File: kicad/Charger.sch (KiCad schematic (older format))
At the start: 14 parts, among them P7 USB_A, P8 BAT1, P9 BAT2, U10 MCP73831, U9 MCP73831

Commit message: 新基板，部品を配置
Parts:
- renumbered D14 to D16, D15 to D17, R23 to R25, R24 to R26, R25 to R27, R26 to R28
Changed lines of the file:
@@
 $EndComp
 $Comp
-L R R25
+L R R27
 U 1 1 58402BC3
 P 4300 4250
-AR Path="/58401A83/58402BC3" Ref="R25"  Part="1"
-AR Path="/58410148/58402BC3" Ref="R29"  Part="1"
-F 0 "R29" V 4380 4250 50  0000 C CNN
+AR Path="/58401A83/58402BC3" Ref="R27"  Part="1"
+AR Path="/58410148/58402BC3" Ref="R31"  Part="1"
+F 0 "R31" V 4380 4250 50  0000 C CNN
 F 1 "4.7k" V 4300 4250 50  0000 C CNN
 F 2 "Resistors_SMD:R_0603" V 4230 4250 50  0001 C CNN
@@
 $EndComp
 $Comp
-L R R23
+L R R25
 U 1 1 58402E63
 P 5650 4000
-AR Path="/58401A83/58402E63" Ref="R23"  Part="1"
-AR Path="/58410148/58402E63" Ref="R27"  Part="1"
-F 0 "R27" V 5730 4000 50  0000 C CNN
+AR Path="/58401A83/58402E63" Ref="R25"  Part="1"
+AR Path="/58410148/58402E63" Ref="R29"  Part="1"
+F 0 "R29" V 5730 4000 50  0000 C CNN
 F 1 "1k" V 5650 4000 50  0000 C CNN
 F 2 "Resistors_SMD:R_0603" V 5580 4000 50  0001 C CNN
@@
 $EndComp
 $Comp
-L LED D14
+L LED D16
 U 1 1 58402EE4
 P 5900 3600
-AR Path="/58401A83/58402EE4" Ref="D14"  Part="1"
-AR Path="/58410148/58402EE4" Ref="D16"  Part="1"
-F 0 "D16" H 5900 3700 50  0000 C CNN
+AR Path="/58401A83/58402EE4" Ref="D16"  Part="1"
+AR Path="/58410148/58402EE4" Ref="D18"  Part="1"
+F 0 "D18" H 5900 3700 50  0000 C CNN
 F 1 "LED" H 5900 3500 50  0000 C CNN
 F 2 "LEDs:LED_0603" H 5900 3600 50  0001 C CNN
@@
 $EndComp
 $Comp
-L R R26
+L R R28
 U 1 1 5840343B
 P 6800 4250
-AR Path="/58401A83/5840343B" Ref="R26"  Part="1"
-AR Path="/58410148/5840343B" Ref="R30"  Part="1"
-F 0 "R30" V 6880 4250 50  0000 C CNN
+AR Path="/58401A83/5840343B" Ref="R28"  Part="1"
+AR Path="/58410148/5840343B" Ref="R32"  Part="1"
+F 0 "R32" V 6880 4250 50  0000 C CNN
 F 1 "4.7k" V 6800 4250 50  0000 C CNN
 F 2 "Resistors_SMD:R_0603" V 6730 4250 50  0001 C CNN
@@
 $EndComp
 $Comp
-L R R24
+L R R26
 U 1 1 58403665
 P 8150 4000
-AR Path="/58401A83/58403665" Ref="R24"  Part="1"
-AR Path="/58410148/58403665" Ref="R28"  Part="1"
-F 0 "R28" V 8230 4000 50  0000 C CNN
+AR Path="/58401A83/58403665" Ref="R26"  Part="1"
+AR Path="/58410148/58403665" Ref="R30"  Part="1"
+F 0 "R30" V 8230 4000 50  0000 C CNN
 F 1 "1k" V 8150 4000 50  0000 C CNN
 F 2 "Resistors_SMD:R_0603" V 8080 4000 50  0001 C CNN
@@
 $EndComp
 $Comp
-L LED D15
+L LED D17
 U 1 1 584036D1
 P 8400 3600
-AR Path="/58401A83/584036D1" Ref="D15"  Part="1"
-AR Path="/58410148/584036D1" Ref="D17"  Part="1"
-F 0 "D17" H 8400 3700 50  0000 C CNN
+AR Path="/58401A83/584036D1" Ref="D17"  Part="1"
+AR Path="/58410148/584036D1" Ref="D19"  Part="1"
+F 0 "D19" H 8400 3700 50  0000 C CNN
 F 1 "LED" H 8400 3500 50  0000 C CNN
 F 2 "LEDs:LED_0603" H 8400 3600 50  0001 C CNN
@@
 NoConn ~ 3800 3500
 $Comp
-L PWR_FLAG #FLG0104
+L PWR_FLAG #FLG0106
 U 1 1 58409F28
 P 3600 4400
-AR Path="/58401A83/58409F28" Ref="#FLG0104"  Part="1"
-AR Path="/58410148/58409F28" Ref="#FLG0106"  Part="1"
-F 0 "#FLG0106" H 3600 4495 50  0001 C CNN
+AR Path="/58401A83/58409F28" Ref="#FLG0106"  Part="1"
+AR Path="/58410148/58409F28" Ref="#FLG0108"  Part="1"
+F 0 "#FLG0108" H 3600 4495 50  0001 C CNN
 F 1 "PWR_FLAG" H 3600 4580 50  0000 C CNN
 F 2 "" H 3600 4400 50  0000 C CNN
@@
 Connection ~ 3600 4500
 $Comp
-L PWR_FLAG #FLG0105
+L PWR_FLAG #FLG0107
 U 1 1 5840A59B
 P 8800 3300
-AR Path="/58401A83/5840A59B" Ref="#FLG0105"  Part="1"
-AR Path="/58410148/5840A59B" Ref="#FLG0107"  Part="1"
-F 0 "#FLG0107" H 8800 3395 50  0001 C CNN
+AR Path="/58401A83/5840A59B" Ref="#FLG0107"  Part="1"
+AR Path="/58410148/5840A59B" Ref="#FLG0109"  Part="1"
+F 0 "#FLG0109" H 8800 3395 50  0001 C CNN
 F 1 "PWR_FLAG" H 8800 3480 50  0000 C CNN
 F 2 "" H 8800 3300 50  0000 C CNN

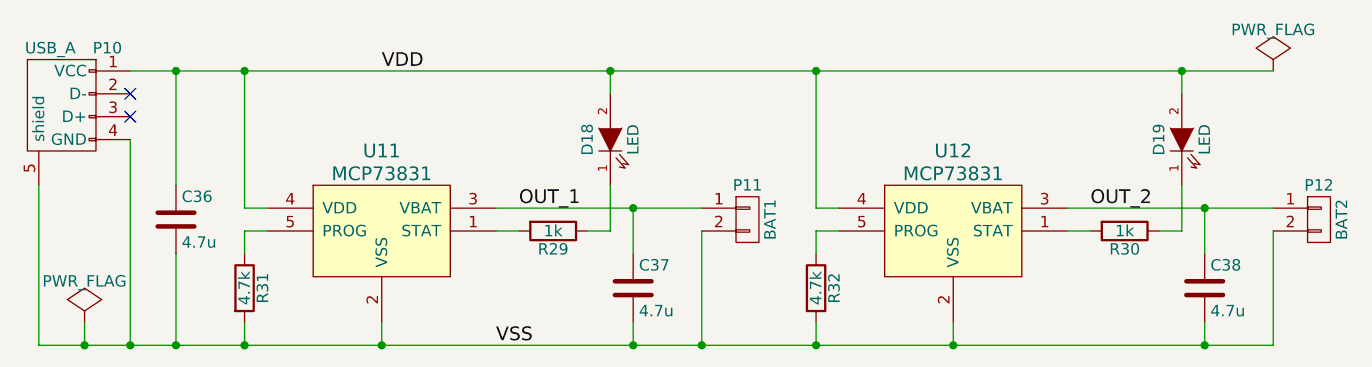
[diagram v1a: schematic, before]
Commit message: 自動配線用にdsn吐き出し
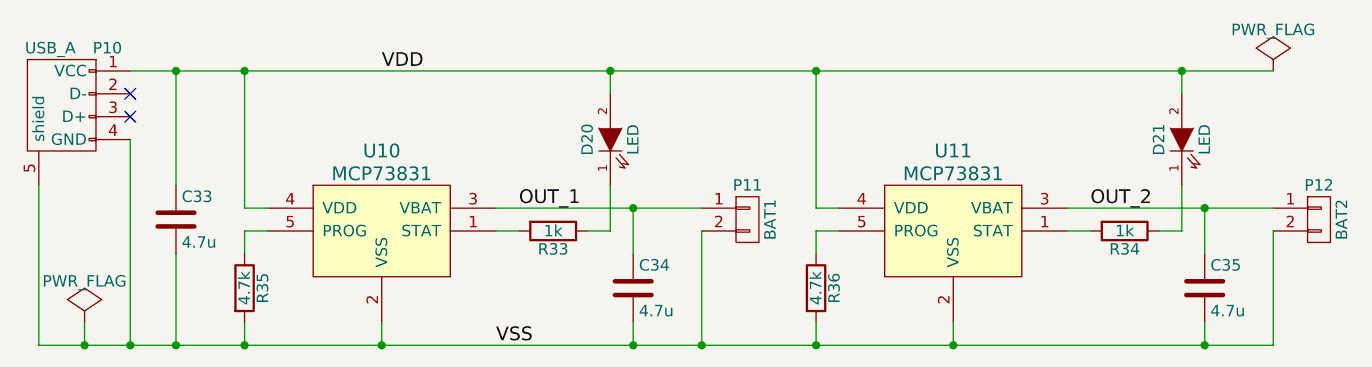
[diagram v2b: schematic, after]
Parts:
- renumbered C33 to C30, C34 to C31, C35 to C32, D16 to D18, D17 to D19, R25 to R29, R26 to R30, R27 to R31, R28 to R32, U9 to U8, U10 to U9
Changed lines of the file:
@@
 $EndComp
 $Comp
-L C C33
+L C C30
 U 1 1 58401C16
 P 4000 3950
-AR Path="/58401A83/58401C16" Ref="C33"  Part="1"
-AR Path="/58410148/58401C16" Ref="C36"  Part="1"
-F 0 "C36" H 4025 4050 50  0000 L CNN
+AR Path="/58401A83/58401C16" Ref="C30"  Part="1"
+AR Path="/58410148/58401C16" Ref="C33"  Part="1"
+F 0 "C33" H 4025 4050 50  0000 L CNN
 F 1 "4.7u" H 4025 3850 50  0000 L CNN
 F 2 "Capacitors_SMD:C_0603" H 4038 3800 50  0001 C CNN
@@
 $EndComp
 $Comp
-L MCP73831 U10
+L MCP73831 U9
 U 1 1 584023C4
 P 7400 4000
-AR Path="/58401A83/584023C4" Ref="U10"  Part="1"
-AR Path="/58410148/584023C4" Ref="U12"  Part="1"
-F 0 "U12" H 7400 4350 60  0000 C CNN
+AR Path="/58401A83/584023C4" Ref="U9"  Part="1"
+AR Path="/58410148/584023C4" Ref="U11"  Part="1"
+F 0 "U11" H 7400 4350 60  0000 C CNN
 F 1 "MCP73831" H 7400 4250 60  0000 C CNN
 F 2 "TO_SOT_Packages_SMD:SOT-23-5" H 7400 4000 60  0001 C CNN
@@
 $EndComp
 $Comp
-L R R27
+L R R31
 U 1 1 58402BC3
 P 4300 4250
-AR Path="/58401A83/58402BC3" Ref="R27"  Part="1"
-AR Path="/58410148/58402BC3" Ref="R31"  Part="1"
-F 0 "R31" V 4380 4250 50  0000 C CNN
+AR Path="/58401A83/58402BC3" Ref="R31"  Part="1"
+AR Path="/58410148/58402BC3" Ref="R35"  Part="1"
+F 0 "R35" V 4380 4250 50  0000 C CNN
 F 1 "4.7k" V 4300 4250 50  0000 C CNN
 F 2 "Resistors_SMD:R_0603" V 4230 4250 50  0001 C CNN
@@
 $EndComp
 $Comp
-L MCP73831 U9
+L MCP73831 U8
 U 1 1 58402CB7
 P 4900 4000
-AR Path="/58401A83/58402CB7" Ref="U9"  Part="1"
-AR Path="/58410148/58402CB7" Ref="U11"  Part="1"
-F 0 "U11" H 4900 4350 60  0000 C CNN
+AR Path="/58401A83/58402CB7" Ref="U8"  Part="1"
+AR Path="/58410148/58402CB7" Ref="U10"  Part="1"
+F 0 "U10" H 4900 4350 60  0000 C CNN
 F 1 "MCP73831" H 4900 4250 60  0000 C CNN
 F 2 "TO_SOT_Packages_SMD:SOT-23-5" H 4900 4000 60  0001 C CNN
@@
 $EndComp
 $Comp
-L R R25
+L R R29
 U 1 1 58402E63
 P 5650 4000
-AR Path="/58401A83/58402E63" Ref="R25"  Part="1"
-AR Path="/58410148/58402E63" Ref="R29"  Part="1"
-F 0 "R29" V 5730 4000 50  0000 C CNN
+AR Path="/58401A83/58402E63" Ref="R29"  Part="1"
+AR Path="/58410148/58402E63" Ref="R33"  Part="1"
+F 0 "R33" V 5730 4000 50  0000 C CNN
 F 1 "1k" V 5650 4000 50  0000 C CNN
 F 2 "Resistors_SMD:R_0603" V 5580 4000 50  0001 C CNN
@@
 $EndComp
 $Comp
-L LED D16
+L LED D18
 U 1 1 58402EE4
 P 5900 3600
-AR Path="/58401A83/58402EE4" Ref="D16"  Part="1"
-AR Path="/58410148/58402EE4" Ref="D18"  Part="1"
-F 0 "D18" H 5900 3700 50  0000 C CNN
+AR Path="/58401A83/58402EE4" Ref="D18"  Part="1"
+AR Path="/58410148/58402EE4" Ref="D20"  Part="1"
+F 0 "D20" H 5900 3700 50  0000 C CNN
 F 1 "LED" H 5900 3500 50  0000 C CNN
 F 2 "LEDs:LED_0603" H 5900 3600 50  0001 C CNN
@@
 $EndComp
 $Comp
-L R R28
+L R R32
 U 1 1 5840343B
 P 6800 4250
-AR Path="/58401A83/5840343B" Ref="R28"  Part="1"
-AR Path="/58410148/5840343B" Ref="R32"  Part="1"
-F 0 "R32" V 6880 4250 50  0000 C CNN
+AR Path="/58401A83/5840343B" Ref="R32"  Part="1"
+AR Path="/58410148/5840343B" Ref="R36"  Part="1"
+F 0 "R36" V 6880 4250 50  0000 C CNN
 F 1 "4.7k" V 6800 4250 50  0000 C CNN
 F 2 "Resistors_SMD:R_0603" V 6730 4250 50  0001 C CNN
@@
 $EndComp
 $Comp
-L R R26
+L R R30
 U 1 1 58403665
 P 8150 4000
-AR Path="/58401A83/58403665" Ref="R26"  Part="1"
-AR Path="/58410148/58403665" Ref="R30"  Part="1"
-F 0 "R30" V 8230 4000 50  0000 C CNN
+AR Path="/58401A83/58403665" Ref="R30"  Part="1"
+AR Path="/58410148/58403665" Ref="R34"  Part="1"
+F 0 "R34" V 8230 4000 50  0000 C CNN
 F 1 "1k" V 8150 4000 50  0000 C CNN
 F 2 "Resistors_SMD:R_0603" V 8080 4000 50  0001 C CNN
@@
 $EndComp
 $Comp
-L LED D17
+L LED D19
 U 1 1 584036D1
 P 8400 3600
-AR Path="/58401A83/584036D1" Ref="D17"  Part="1"
-AR Path="/58410148/584036D1" Ref="D19"  Part="1"
-F 0 "D19" H 8400 3700 50  0000 C CNN
+AR Path="/58401A83/584036D1" Ref="D19"  Part="1"
+AR Path="/58410148/584036D1" Ref="D21"  Part="1"
+F 0 "D21" H 8400 3700 50  0000 C CNN
 F 1 "LED" H 8400 3500 50  0000 C CNN
 F 2 "LEDs:LED_0603" H 8400 3600 50  0001 C CNN
@@
 $EndComp
 $Comp
-L C C34
+L C C31
 U 1 1 5840663C
 P 6000 4250
-AR Path="/58401A83/5840663C" Ref="C34"  Part="1"
-AR Path="/58410148/5840663C" Ref="C37"  Part="1"
-F 0 "C37" H 6025 4350 50  0000 L CNN
+AR Path="/58401A83/5840663C" Ref="C31"  Part="1"
+AR Path="/58410148/5840663C" Ref="C34"  Part="1"
+F 0 "C34" H 6025 4350 50  0000 L CNN
 F 1 "4.7u" H 6025 4150 50  0000 L CNN
 F 2 "Capacitors_SMD:C_0603" H 6038 4100 50  0001 C CNN
@@
 	3400 4500 8800 4500
 $Comp
-L C C35
+L C C32
 U 1 1 58406E3A
 P 8500 4250
-AR Path="/58401A83/58406E3A" Ref="C35"  Part="1"
-AR Path="/58410148/58406E3A" Ref="C38"  Part="1"
-F 0 "C38" H 8525 4350 50  0000 L CNN
+AR Path="/58401A83/58406E3A" Ref="C32"  Part="1"
+AR Path="/58410148/58406E3A" Ref="C35"  Part="1"
+F 0 "C35" H 8525 4350 50  0000 L CNN
 F 1 "4.7u" H 8525 4150 50  0000 L CNN
 F 2 "Capacitors_SMD:C_0603" H 8538 4100 50  0001 C CNN
@@
 NoConn ~ 3800 3500
 $Comp
-L PWR_FLAG #FLG0106
+L PWR_FLAG #FLG0104
 U 1 1 58409F28
 P 3600 4400
-AR Path="/58401A83/58409F28" Ref="#FLG0106"  Part="1"
-AR Path="/58410148/58409F28" Ref="#FLG0108"  Part="1"
-F 0 "#FLG0108" H 3600 4495 50  0001 C CNN
+AR Path="/58401A83/58409F28" Ref="#FLG0104"  Part="1"
+AR Path="/58410148/58409F28" Ref="#FLG0106"  Part="1"
+F 0 "#FLG0106" H 3600 4495 50  0001 C CNN
 F 1 "PWR_FLAG" H 3600 4580 50  0000 C CNN
 F 2 "" H 3600 4400 50  0000 C CNN
@@
 Connection ~ 3600 4500
 $Comp
-L PWR_FLAG #FLG0107
+L PWR_FLAG #FLG0105
 U 1 1 5840A59B
 P 8800 3300
-AR Path="/58401A83/5840A59B" Ref="#FLG0107"  Part="1"
-AR Path="/58410148/5840A59B" Ref="#FLG0109"  Part="1"
-F 0 "#FLG0109" H 8800 3395 50  0001 C CNN
+AR Path="/58401A83/5840A59B" Ref="#FLG0105"  Part="1"
+AR Path="/58410148/5840A59B" Ref="#FLG0107"  Part="1"
+F 0 "#FLG0107" H 8800 3395 50  0001 C CNN
 F 1 "PWR_FLAG" H 8800 3480 50  0000 C CNN
 F 2 "" H 8800 3300 50  0000 C CNN
